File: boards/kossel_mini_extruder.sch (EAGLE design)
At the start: 26 parts

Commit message: still grinding on board
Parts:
- removed LED10, LED8, LED9: (no value), SparkFun-LED:LED0805
- removed R10, R8, R9: (no value), SparkFun-Passives:RESISTOR0805-RES
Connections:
- removed net N$13: LED9.C, R9.2
- removed net N$14: LED10.C, R10.2
- removed net N$9: LED8.C, R8.2
- net GND: no longer R10.1, R8.1, R9.1
- net VCC: no longer LED10.A, LED8.A, LED9.A
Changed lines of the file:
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@@
 <part name="R5" library="SparkFun-Passives" deviceset="RESISTOR" device="0805-RES"/>
 <part name="R6" library="SparkFun-Passives" deviceset="RESISTOR" device="0805-RES"/>
-<part name="GND1" library="SparkFun-Aesthetics" deviceset="GND" device=""/>
-<part name="GND3" library="SparkFun-Aesthetics" deviceset="GND" device=""/>
-<part name="LED8" library="SparkFun-LED" deviceset="LED" device="0805"/>
-<part name="LED9" library="SparkFun-LED" deviceset="LED" device="0805"/>
-<part name="LED10" library="SparkFun-LED" deviceset="LED" device="0805"/>
-<part name="R8" library="SparkFun-Passives" deviceset="RESISTOR" device="0805-RES"/>
-<part name="R9" library="SparkFun-Passives" deviceset="RESISTOR" device="0805-RES"/>
-<part name="R10" library="SparkFun-Passives" deviceset="RESISTOR" device="0805-RES"/>
-<part name="GND5" library="SparkFun-Aesthetics" deviceset="GND" device=""/>
 <part name="LED11" library="SparkFun-LED" deviceset="LED" device="0805"/>
 <part name="LED12" library="SparkFun-LED" deviceset="LED" device="0805"/>
@@
 <instance part="R5" gate="G$1" x="-2.54" y="55.88" rot="R90"/>
 <instance part="R6" gate="G$1" x="7.62" y="55.88" rot="R90"/>
-<instance part="GND1" gate="1" x="22.86" y="50.8"/>
-<instance part="GND3" gate="1" x="-17.78" y="43.18"/>
-<instance part="LED8" gate="G$1" x="-12.7" y="33.02"/>
-<instance part="LED9" gate="G$1" x="-2.54" y="33.02"/>
-<instance part="LED10" gate="G$1" x="7.62" y="33.02"/>
-<instance part="R8" gate="G$1" x="-12.7" y="17.78" rot="R90"/>
-<instance part="R9" gate="G$1" x="-2.54" y="17.78" rot="R90"/>
-<instance part="R10" gate="G$1" x="7.62" y="17.78" rot="R90"/>
-<instance part="GND5" gate="1" x="-17.78" y="5.08"/>
 <instance part="LED11" gate="G$1" x="-22.86" y="116.84"/>
 <instance part="LED12" gate="G$1" x="-12.7" y="116.84"/>
@@
 </segment>
 </net>
-<net name="GND" class="0">
-<segment>
-<pinref part="R1" gate="G$1" pin="1"/>
-<wire x1="-43.18" y1="50.8" x2="-43.18" y2="48.26" width="0.1524" layer="91"/>
-<wire x1="-43.18" y1="48.26" x2="-33.02" y2="48.26" width="0.1524" layer="91"/>
-<pinref part="GND3" gate="1" pin="GND"/>
-<wire x1="-33.02" y1="48.26" x2="-22.86" y2="48.26" width="0.1524" layer="91"/>
-<wire x1="-22.86" y1="48.26" x2="-17.78" y2="48.26" width="0.1524" layer="91"/>
-<wire x1="-17.78" y1="48.26" x2="-17.78" y2="45.72" width="0.1524" layer="91"/>
-<pinref part="R6" gate="G$1" pin="1"/>
-<wire x1="7.62" y1="50.8" x2="7.62" y2="48.26" width="0.1524" layer="91"/>
-<wire x1="7.62" y1="48.26" x2="-2.54" y2="48.26" width="0.1524" layer="91"/>
-<junction x="-17.78" y="48.26"/>
-<pinref part="R5" gate="G$1" pin="1"/>
-<wire x1="-2.54" y1="48.26" x2="-12.7" y2="48.26" width="0.1524" layer="91"/>
-<wire x1="-12.7" y1="48.26" x2="-17.78" y2="48.26" width="0.1524" layer="91"/>
-<wire x1="-2.54" y1="50.8" x2="-2.54" y2="48.26" width="0.1524" layer="91"/>
-<junction x="-2.54" y="48.26"/>
-<pinref part="R4" gate="G$1" pin="1"/>
-<wire x1="-12.7" y1="50.8" x2="-12.7" y2="48.26" width="0.1524" layer="91"/>
-<junction x="-12.7" y="48.26"/>
-<pinref part="R3" gate="G$1" pin="1"/>
-<wire x1="-22.86" y1="50.8" x2="-22.86" y2="48.26" width="0.1524" layer="91"/>
-<junction x="-22.86" y="48.26"/>
-<pinref part="R2" gate="G$1" pin="1"/>
-<wire x1="-33.02" y1="50.8" x2="-33.02" y2="48.26" width="0.1524" layer="91"/>
-<junction x="-33.02" y="48.26"/>
-</segment>
-<segment>
-<pinref part="GND5" gate="1" pin="GND"/>
-<wire x1="-17.78" y1="10.16" x2="-17.78" y2="7.62" width="0.1524" layer="91"/>
-<pinref part="R10" gate="G$1" pin="1"/>
-<wire x1="7.62" y1="12.7" x2="7.62" y2="10.16" width="0.1524" layer="91"/>
-<wire x1="7.62" y1="10.16" x2="-2.54" y2="10.16" width="0.1524" layer="91"/>
-<pinref part="R9" gate="G$1" pin="1"/>
-<wire x1="-2.54" y1="10.16" x2="-12.7" y2="10.16" width="0.1524" layer="91"/>
-<wire x1="-12.7" y1="10.16" x2="-17.78" y2="10.16" width="0.1524" layer="91"/>
-<wire x1="-2.54" y1="12.7" x2="-2.54" y2="10.16" width="0.1524" layer="91"/>
-<junction x="-2.54" y="10.16"/>
-<pinref part="R8" gate="G$1" pin="1"/>
-<wire x1="-12.7" y1="12.7" x2="-12.7" y2="10.16" width="0.1524" layer="91"/>
-<junction x="-12.7" y="10.16"/>
-</segment>
-<segment>
-<pinref part="GND1" gate="1" pin="GND"/>
-<wire x1="22.86" y1="53.34" x2="22.86" y2="73.66" width="0.1524" layer="91"/>
-<pinref part="SV2" gate="1" pin="4"/>
-<wire x1="22.86" y1="73.66" x2="30.48" y2="73.66" width="0.1524" layer="91"/>
-</segment>
-</net>
-<net name="N$9" class="0">
-<segment>
-<pinref part="LED8" gate="G$1" pin="C"/>
-<pinref part="R8" gate="G$1" pin="2"/>
-<wire x1="-12.7" y1="27.94" x2="-12.7" y2="22.86" width="0.1524" layer="91"/>
-</segment>
-</net>
-<net name="N$13" class="0">
-<segment>
-<pinref part="LED9" gate="G$1" pin="C"/>
-<pinref part="R9" gate="G$1" pin="2"/>
-<wire x1="-2.54" y1="27.94" x2="-2.54" y2="22.86" width="0.1524" layer="91"/>
-</segment>
-</net>
-<net name="N$14" class="0">
-<segment>
-<pinref part="LED10" gate="G$1" pin="C"/>
-<pinref part="R10" gate="G$1" pin="2"/>
-<wire x1="7.62" y1="27.94" x2="7.62" y2="22.86" width="0.1524" layer="91"/>
-</segment>
-</net>
 <net name="VCC" class="0">
 <segment>
-<pinref part="LED10" gate="G$1" pin="A"/>
-<wire x1="-12.7" y1="38.1" x2="-2.54" y2="38.1" width="0.1524" layer="91"/>
-<wire x1="-2.54" y1="38.1" x2="7.62" y2="38.1" width="0.1524" layer="91"/>
-<wire x1="7.62" y1="38.1" x2="7.62" y2="35.56" width="0.1524" layer="91"/>
-<pinref part="LED9" gate="G$1" pin="A"/>
-<wire x1="-2.54" y1="35.56" x2="-2.54" y2="38.1" width="0.1524" layer="91"/>
-<junction x="-2.54" y="38.1"/>
-<pinref part="LED8" gate="G$1" pin="A"/>
-<wire x1="-12.7" y1="35.56" x2="-12.7" y2="38.1" width="0.1524" layer="91"/>
-<wire x1="7.62" y1="38.1" x2="15.24" y2="38.1" width="0.1524" layer="91"/>
-<junction x="7.62" y="38.1"/>
 <pinref part="LED1" gate="G$1" pin="A"/>
 <wire x1="-43.18" y1="73.66" x2="-43.18" y2="76.2" width="0.1524" layer="91"/>
@@
 <wire x1="-33.02" y1="73.66" x2="-33.02" y2="76.2" width="0.1524" layer="91"/>
 <junction x="-33.02" y="76.2"/>
-<wire x1="7.62" y1="76.2" x2="15.24" y2="76.2" width="0.1524" layer="91"/>
 <junction x="7.62" y="76.2"/>
-<wire x1="15.24" y1="38.1" x2="15.24" y2="76.2" width="0.1524" layer="91"/>
-<junction x="15.24" y="76.2"/>
 <pinref part="SV2" gate="1" pin="6"/>
-<wire x1="15.24" y1="76.2" x2="30.48" y2="76.2" width="0.1524" layer="91"/>
+<wire x1="7.62" y1="76.2" x2="30.48" y2="76.2" width="0.1524" layer="91"/>
 </segment>
 </net>
@@
 </segment>
 </net>
+<net name="GND" class="0">
+<segment>
+<pinref part="R1" gate="G$1" pin="1"/>
+<wire x1="-43.18" y1="50.8" x2="-43.18" y2="48.26" width="0.1524" layer="91"/>
+<wire x1="-43.18" y1="48.26" x2="-33.02" y2="48.26" width="0.1524" layer="91"/>
+<wire x1="-33.02" y1="48.26" x2="-22.86" y2="48.26" width="0.1524" layer="91"/>
+<pinref part="R6" gate="G$1" pin="1"/>
+<wire x1="7.62" y1="50.8" x2="7.62" y2="48.26" width="0.1524" layer="91"/>
+<wire x1="7.62" y1="48.26" x2="-2.54" y2="48.26" width="0.1524" layer="91"/>
+<pinref part="R5" gate="G$1" pin="1"/>
+<wire x1="-2.54" y1="48.26" x2="-12.7" y2="48.26" width="0.1524" layer="91"/>
+<wire x1="-12.7" y1="48.26" x2="-22.86" y2="48.26" width="0.1524" layer="91"/>
+<wire x1="-2.54" y1="50.8" x2="-2.54" y2="48.26" width="0.1524" layer="91"/>
+<junction x="-2.54" y="48.26"/>
+<pinref part="R4" gate="G$1" pin="1"/>
+<wire x1="-12.7" y1="50.8" x2="-12.7" y2="48.26" width="0.1524" layer="91"/>
+<junction x="-12.7" y="48.26"/>
+<pinref part="R3" gate="G$1" pin="1"/>
+<wire x1="-22.86" y1="50.8" x2="-22.86" y2="48.26" width="0.1524" layer="91"/>
+<junction x="-22.86" y="48.26"/>
+<pinref part="R2" gate="G$1" pin="1"/>
+<wire x1="-33.02" y1="50.8" x2="-33.02" y2="48.26" width="0.1524" layer="91"/>
+<junction x="-33.02" y="48.26"/>
+<junction x="7.62" y="48.26"/>
+<wire x1="7.62" y1="48.26" x2="15.24" y2="48.26" width="0.1524" layer="91"/>
+<wire x1="15.24" y1="48.26" x2="15.24" y2="73.66" width="0.1524" layer="91"/>
+<pinref part="SV2" gate="1" pin="4"/>
+<wire x1="15.24" y1="73.66" x2="30.48" y2="73.66" width="0.1524" layer="91"/>
+</segment>
+</net>

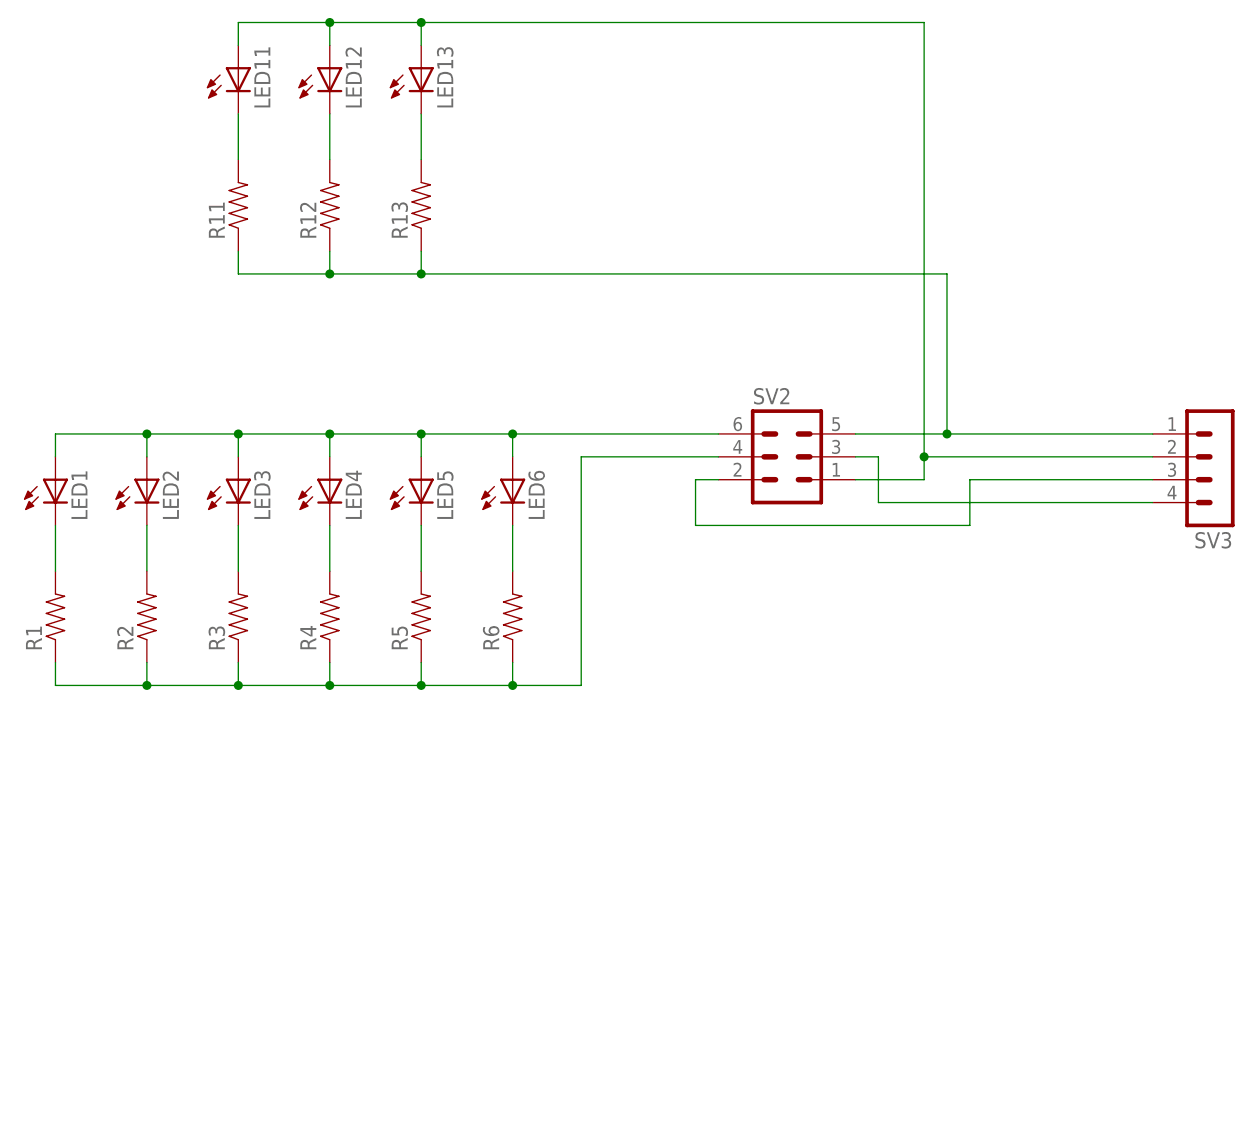
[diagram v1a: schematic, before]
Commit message: first version of new extruder board
and golden dog fan mount
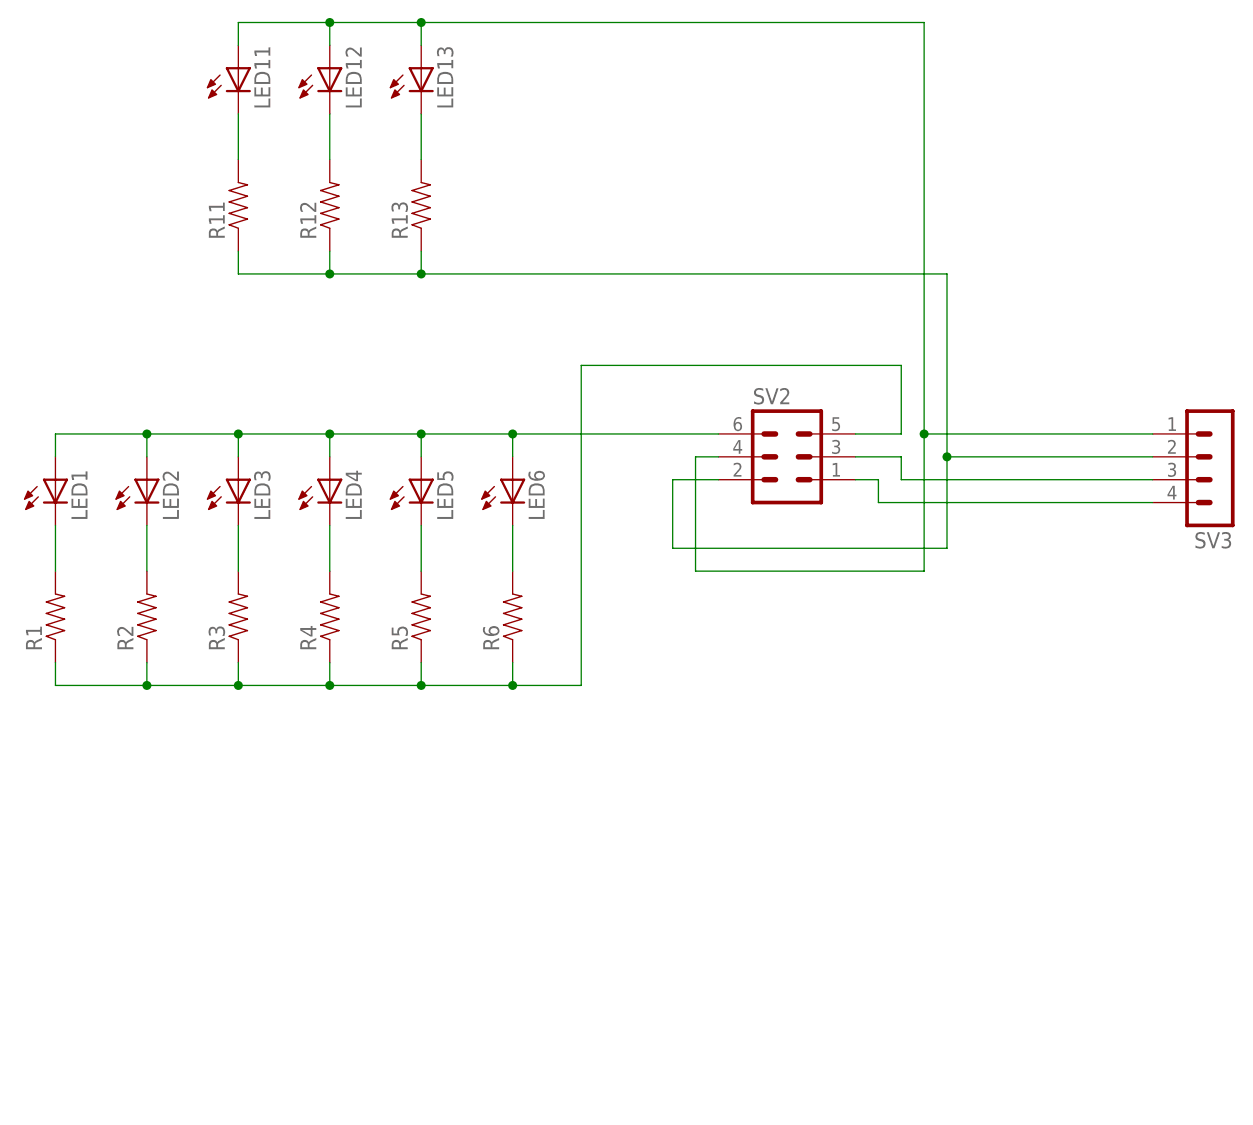
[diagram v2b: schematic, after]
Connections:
- net GND: now also SV2.5; no longer SV2.4
- net HOT_12V: now also SV2.2, SV3.2; no longer SV2.5, SV3.1
- net HOT_SIG: now also SV2.4, SV3.1; no longer SV2.1, SV3.2
- net THERM_GND: now also SV2.1; no longer SV2.3
- net THERM_SIG: now also SV2.3; no longer SV2.2
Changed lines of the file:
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@@
 <?xml version="1.0" encoding="utf-8"?>
 <!DOCTYPE eagle SYSTEM "eagle.dtd">
-<eagle version="6.5.0">
+<eagle version="6.4">
 <drawing>
 <settings>
@@
 <junction x="-33.02" y="76.2"/>
 <junction x="7.62" y="76.2"/>
+<wire x1="30.48" y1="76.2" x2="7.62" y2="76.2" width="0.1524" layer="91"/>
 <pinref part="SV2" gate="1" pin="6"/>
-<wire x1="7.62" y1="76.2" x2="30.48" y2="76.2" width="0.1524" layer="91"/>
 </segment>
 </net>
 <net name="THERM_GND" class="0">
 <segment>
-<pinref part="SV2" gate="1" pin="3"/>
-<wire x1="45.72" y1="73.66" x2="48.26" y2="73.66" width="0.1524" layer="91"/>
-<wire x1="48.26" y1="73.66" x2="48.26" y2="68.58" width="0.1524" layer="91"/>
 <pinref part="SV3" gate="1" pin="4"/>
 <wire x1="48.26" y1="68.58" x2="78.74" y2="68.58" width="0.1524" layer="91"/>
+<wire x1="48.26" y1="68.58" x2="48.26" y2="71.12" width="0.1524" layer="91"/>
+<pinref part="SV2" gate="1" pin="1"/>
+<wire x1="48.26" y1="71.12" x2="45.72" y2="71.12" width="0.1524" layer="91"/>
 </segment>
 </net>
@@
 <wire x1="53.34" y1="121.92" x2="-2.54" y2="121.92" width="0.1524" layer="91"/>
 <junction x="-2.54" y="121.92"/>
-<wire x1="53.34" y1="121.92" x2="53.34" y2="73.66" width="0.1524" layer="91"/>
-<pinref part="SV2" gate="1" pin="1"/>
-<wire x1="53.34" y1="73.66" x2="53.34" y2="71.12" width="0.1524" layer="91"/>
-<wire x1="45.72" y1="71.12" x2="53.34" y2="71.12" width="0.1524" layer="91"/>
-<junction x="53.34" y="73.66"/>
-<pinref part="SV3" gate="1" pin="2"/>
-<wire x1="53.34" y1="73.66" x2="78.74" y2="73.66" width="0.1524" layer="91"/>
+<wire x1="53.34" y1="121.92" x2="53.34" y2="76.2" width="0.1524" layer="91"/>
+<wire x1="53.34" y1="76.2" x2="53.34" y2="60.96" width="0.1524" layer="91"/>
+<wire x1="53.34" y1="60.96" x2="27.94" y2="60.96" width="0.1524" layer="91"/>
+<junction x="53.34" y="76.2"/>
+<pinref part="SV3" gate="1" pin="1"/>
+<wire x1="53.34" y1="76.2" x2="78.74" y2="76.2" width="0.1524" layer="91"/>
+<wire x1="27.94" y1="60.96" x2="27.94" y2="73.66" width="0.1524" layer="91"/>
+<pinref part="SV2" gate="1" pin="4"/>
+<wire x1="27.94" y1="73.66" x2="30.48" y2="73.66" width="0.1524" layer="91"/>
 </segment>
 </net>
@@
 <junction x="-12.7" y="93.98"/>
 <wire x1="-2.54" y1="93.98" x2="55.88" y2="93.98" width="0.1524" layer="91"/>
-<wire x1="55.88" y1="93.98" x2="55.88" y2="76.2" width="0.1524" layer="91"/>
+<wire x1="55.88" y1="93.98" x2="55.88" y2="73.66" width="0.1524" layer="91"/>
 <junction x="-2.54" y="93.98"/>
-<pinref part="SV2" gate="1" pin="5"/>
-<wire x1="55.88" y1="76.2" x2="45.72" y2="76.2" width="0.1524" layer="91"/>
-<junction x="55.88" y="76.2"/>
-<pinref part="SV3" gate="1" pin="1"/>
-<wire x1="55.88" y1="76.2" x2="78.74" y2="76.2" width="0.1524" layer="91"/>
+<wire x1="55.88" y1="73.66" x2="55.88" y2="63.5" width="0.1524" layer="91"/>
+<wire x1="25.4" y1="63.5" x2="55.88" y2="63.5" width="0.1524" layer="91"/>
+<pinref part="SV2" gate="1" pin="2"/>
+<wire x1="30.48" y1="71.12" x2="25.4" y2="71.12" width="0.1524" layer="91"/>
+<wire x1="25.4" y1="71.12" x2="25.4" y2="63.5" width="0.1524" layer="91"/>
+<junction x="55.88" y="73.66"/>
+<pinref part="SV3" gate="1" pin="2"/>
+<wire x1="55.88" y1="73.66" x2="78.74" y2="73.66" width="0.1524" layer="91"/>
 </segment>
 </net>
 <net name="THERM_SIG" class="0">
 <segment>
-<pinref part="SV2" gate="1" pin="2"/>
-<wire x1="27.94" y1="71.12" x2="30.48" y2="71.12" width="0.1524" layer="91"/>
-<wire x1="27.94" y1="71.12" x2="27.94" y2="66.04" width="0.1524" layer="91"/>
-<wire x1="27.94" y1="66.04" x2="58.42" y2="66.04" width="0.1524" layer="91"/>
-<wire x1="58.42" y1="66.04" x2="58.42" y2="71.12" width="0.1524" layer="91"/>
 <pinref part="SV3" gate="1" pin="3"/>
-<wire x1="58.42" y1="71.12" x2="78.74" y2="71.12" width="0.1524" layer="91"/>
+<wire x1="50.8" y1="71.12" x2="78.74" y2="71.12" width="0.1524" layer="91"/>
+<wire x1="50.8" y1="71.12" x2="50.8" y2="73.66" width="0.1524" layer="91"/>
+<pinref part="SV2" gate="1" pin="3"/>
+<wire x1="50.8" y1="73.66" x2="45.72" y2="73.66" width="0.1524" layer="91"/>
 </segment>
 </net>
@@
 <junction x="7.62" y="48.26"/>
 <wire x1="7.62" y1="48.26" x2="15.24" y2="48.26" width="0.1524" layer="91"/>
-<wire x1="15.24" y1="48.26" x2="15.24" y2="73.66" width="0.1524" layer="91"/>
-<pinref part="SV2" gate="1" pin="4"/>
-<wire x1="15.24" y1="73.66" x2="30.48" y2="73.66" width="0.1524" layer="91"/>
-</segment>
-</net>
+<wire x1="15.24" y1="48.26" x2="15.24" y2="83.82" width="0.1524" layer="91"/>
+<wire x1="15.24" y1="83.82" x2="50.8" y2="83.82" width="0.1524" layer="91"/>
+<wire x1="50.8" y1="83.82" x2="50.8" y2="76.2" width="0.1524" layer="91"/>
+<pinref part="SV2" gate="1" pin="5"/>
+<wire x1="50.8" y1="76.2" x2="45.72" y2="76.2" width="0.1524" layer="91"/>
+</segment>
+</net>
